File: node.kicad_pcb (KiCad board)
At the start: 2 copper layers, 46 x 38 mm, 39 parts, among them J1 USB_B_Mini, J2 TC2030_NL, J3 FFC-0.5MM-6POS, J4 Port_1, J5 Port_2, J6 FFC-0.5MM-6POS, J7 Port_3, J8 Port_4, U1 PMIC-LDO-XC6204B332MR_SOT23-5_, U2 LP2985-5.0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

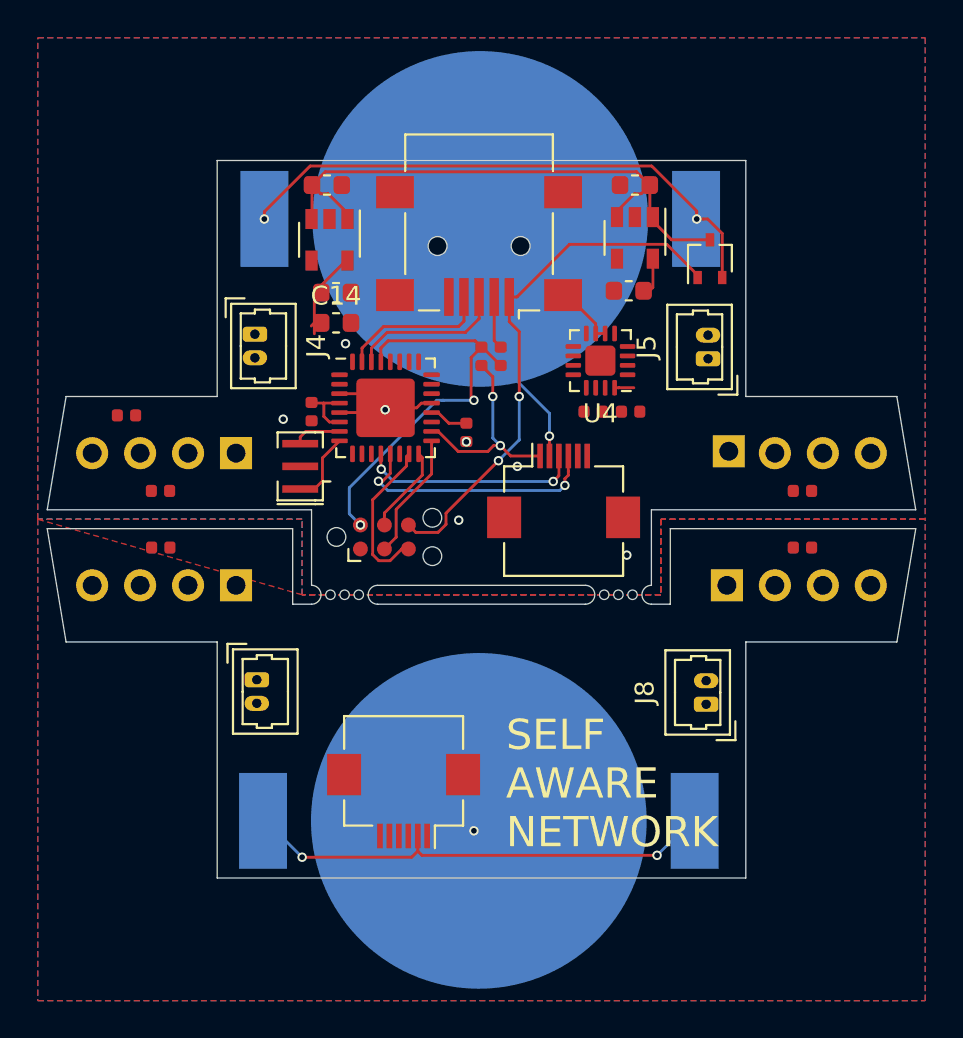
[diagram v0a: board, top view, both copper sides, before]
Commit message: Route top board
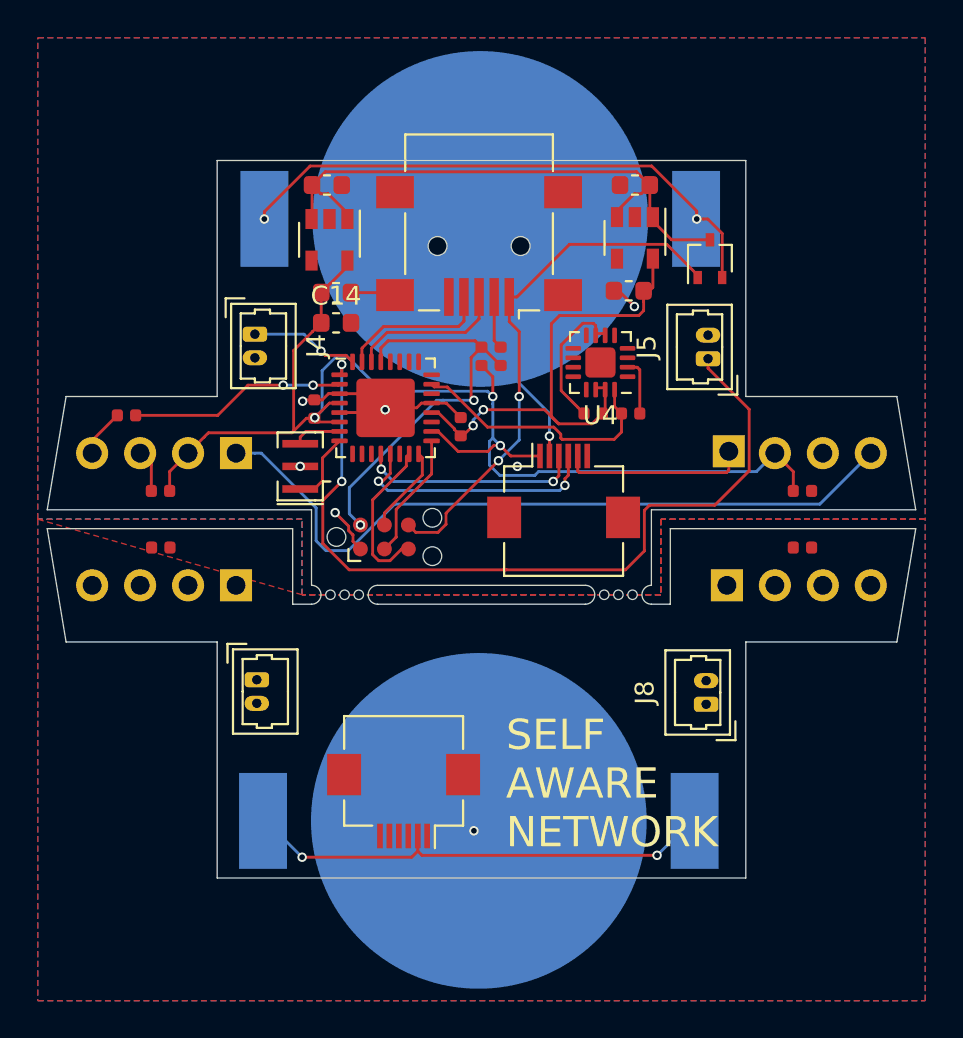
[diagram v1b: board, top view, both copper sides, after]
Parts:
- moved C5 0.42 mm to (145.9, 77.6), turned to 90 degrees
- moved C6 0.20 mm to (138.2, 76.7), turned to 90 degrees
- moved C10 0.10 mm to (154.9, 76.9)
- moved C8 0.10 mm to (152.9, 76.9)
- moved U4 0.10 mm to (153.3, 74.2)
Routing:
- net +5V: track 19.3 -> 67.1 mm, vias 2 -> 3
- net /Top Hemisphere/BNC-2: track 0.00 -> 44.1 mm, vias 0 -> 2
- net Net-(D2-Pad1): track 0.00 -> 38.9 mm
- net +3V3: track 3.85 -> 26.3 mm, vias 0 -> 2
- net GND: track 11.2 -> 30.9 mm, vias 7 -> 6
- net /Top Hemisphere/Z-ACCEL: track 1.02 -> 14.0 mm
- net Net-(R2-Pad2): track 0.00 -> 11.5 mm, vias 0 -> 2
- net /Top Hemisphere/DOUT-BOT: track 0.00 -> 9.89 mm
- net /Top Hemisphere/BNC-1: track 0.00 -> 5.78 mm, vias 0 -> 1
- net /Top Hemisphere/DIN-TOP: track 0.00 -> 2.55 mm

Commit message: Finish routing
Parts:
- moved Y1 0.40 mm to (137.0, 79.7)
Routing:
- net +5VB: track 0.00 -> 48.9 mm
- net Net-(D4-Pad1): track 0.00 -> 34.6 mm
- net /Bottom hemisphere/BNC-4: track 0.00 -> 27.9 mm, vias 0 -> 1
- net /Bottom hemisphere/DIN-BOT: track 0.00 -> 22.9 mm
- net /Bottom hemisphere/BNC-3: track 0.00 -> 13.4 mm
- net GNDB: track 0.00 -> 4.50 mm
- net Net-(D2-Pad1): track 38.9 -> 35.5 mm
- net GND: track 30.9 -> 31.2 mm, vias 6 -> 11

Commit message: Reload footprints (without change)
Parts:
- U1: value PMIC-LDO-XC6204B332MR_SOT23-5_ -> PMIC-LDO-XC6204B332MR_SOT23-5
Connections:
- net /Bottom hemisphere/DIN-BOT renamed /Bottom hemisphere/DOUT
- net /Top Hemisphere/DOUT-BOT renamed /Top Hemisphere/DOUT
